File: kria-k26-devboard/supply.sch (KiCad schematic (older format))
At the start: 0 parts

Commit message: Progress on Debug sheet
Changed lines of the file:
@@
 F1 "usbc-socket.sch" 50
 F2 "PD_CC[1..2]" I L 3600 2800 50
-F3 "DBG_USB[0..1]" I L 3600 2900 50
-F4 "VBUS" I R 4700 2800 50
+F3 "VBUS" I R 4700 2800 50
+F4 "DBG_USB_P" I L 3600 3000 50
+F5 "DBG_USB_N" I L 3600 3100 50
 $EndSheet
 $Sheet
@@
 Text HLabel 3450 2800 0    50   Input ~ 0
 PD_CC[1..2]
-Text HLabel 3450 2900 0    50   Input ~ 0
-DBG_USB[0..1]
 Wire Wire Line
 	3450 2800 3600 2800
-Wire Wire Line
-	3600 2900 3450 2900
 Text HLabel 7550 3550 0    50   Input ~ 0
 VCCOEN_PS_M2C
@@
 Wire Bus Line
 	3400 4600 3600 4600
+Text HLabel 3450 3000 0    50   Input ~ 0
+DBG_USB_P
+Wire Wire Line
+	3450 3000 3600 3000
+Text HLabel 3450 3100 0    50   Input ~ 0
+DBG_USB_N
+Wire Wire Line
+	3450 3100 3600 3100
 $EndSCHEMATC

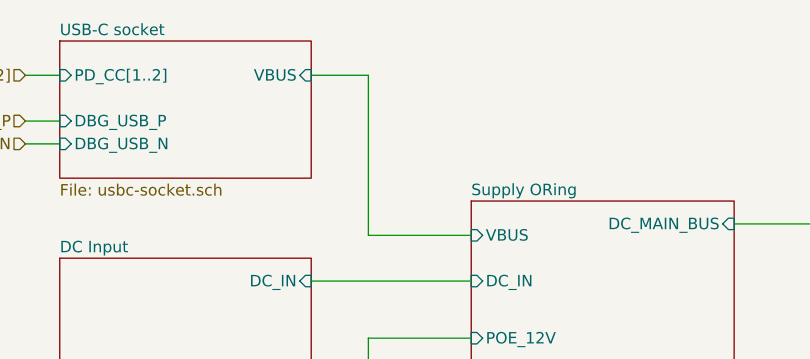
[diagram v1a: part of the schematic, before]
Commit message: Finished Debug and JTAG schematic
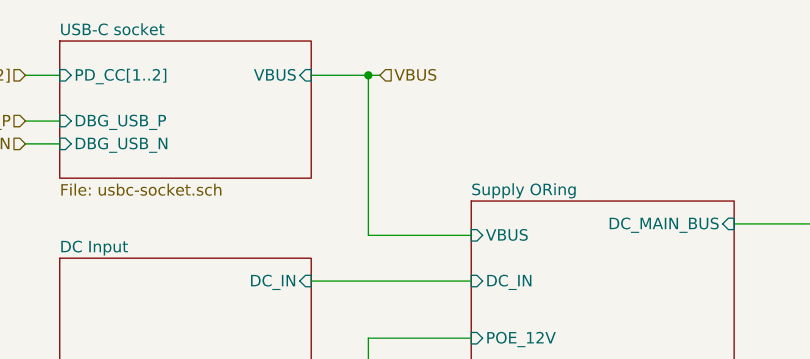
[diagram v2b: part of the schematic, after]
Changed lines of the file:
@@
 Wire Wire Line
 	3450 3100 3600 3100
+Text HLabel 5000 2800 2    50   Input ~ 0
+VBUS
+Wire Wire Line
+	4950 2800 5000 2800
+Connection ~ 4950 2800
 $EndSCHEMATC

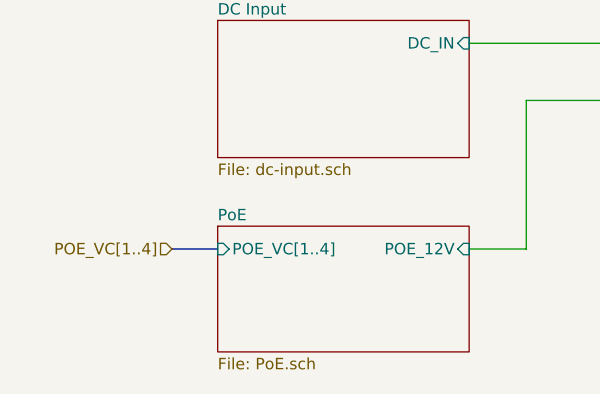
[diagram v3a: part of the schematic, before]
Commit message: Added second ETH interface, connect POE PSE
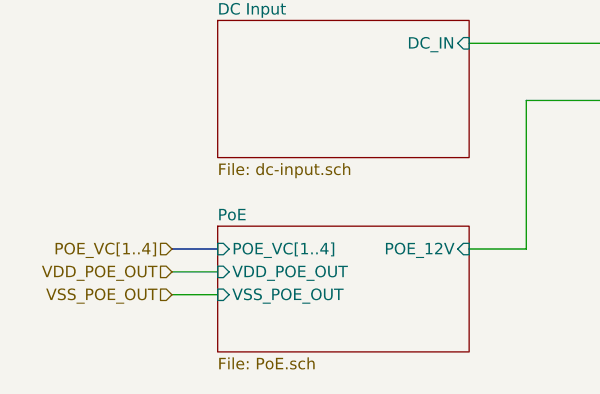
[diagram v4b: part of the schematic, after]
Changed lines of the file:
@@
 F2 "POE_12V" I R 4700 4600 50
 F3 "POE_VC[1..4]" I L 3600 4600 50
+F4 "VDD_POE_OUT" I L 3600 4700 50
+F5 "VSS_POE_OUT" I L 3600 4800 50
 $EndSheet
 $Sheet
@@
 	4950 2800 5000 2800
 Connection ~ 4950 2800
+Wire Wire Line
+	3600 4700 3400 4700
+Wire Wire Line
+	3600 4800 3400 4800
+Text HLabel 3400 4700 0    50   Input ~ 0
+VDD_POE_OUT
+Text HLabel 3400 4800 0    50   Input ~ 0
+VSS_POE_OUT
 $EndSCHEMATC

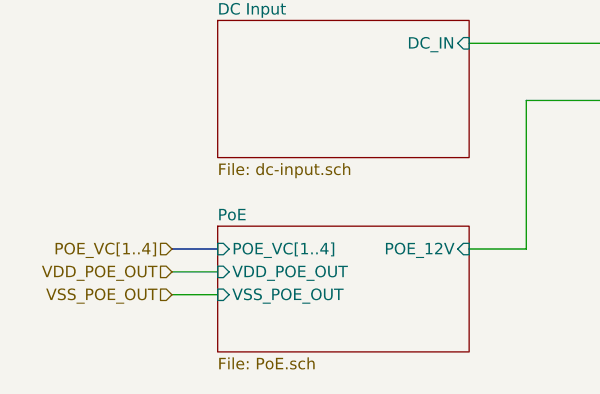
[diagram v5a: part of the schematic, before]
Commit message: Removed PoE PSE and second ETH interface
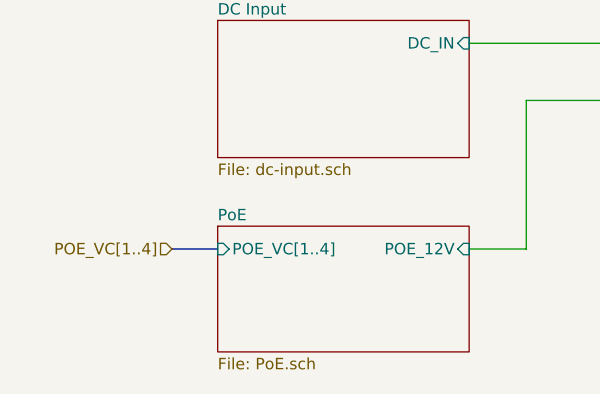
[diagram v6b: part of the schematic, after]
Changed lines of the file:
@@
 F2 "POE_12V" I R 4700 4600 50
 F3 "POE_VC[1..4]" I L 3600 4600 50
-F4 "VDD_POE_OUT" I L 3600 4700 50
-F5 "VSS_POE_OUT" I L 3600 4800 50
 $EndSheet
 $Sheet
@@
 	4950 2800 5000 2800
 Connection ~ 4950 2800
-Wire Wire Line
-	3600 4700 3400 4700
-Wire Wire Line
-	3600 4800 3400 4800
-Text HLabel 3400 4700 0    50   Input ~ 0
-VDD_POE_OUT
-Text HLabel 3400 4800 0    50   Input ~ 0
-VSS_POE_OUT
 $EndSCHEMATC

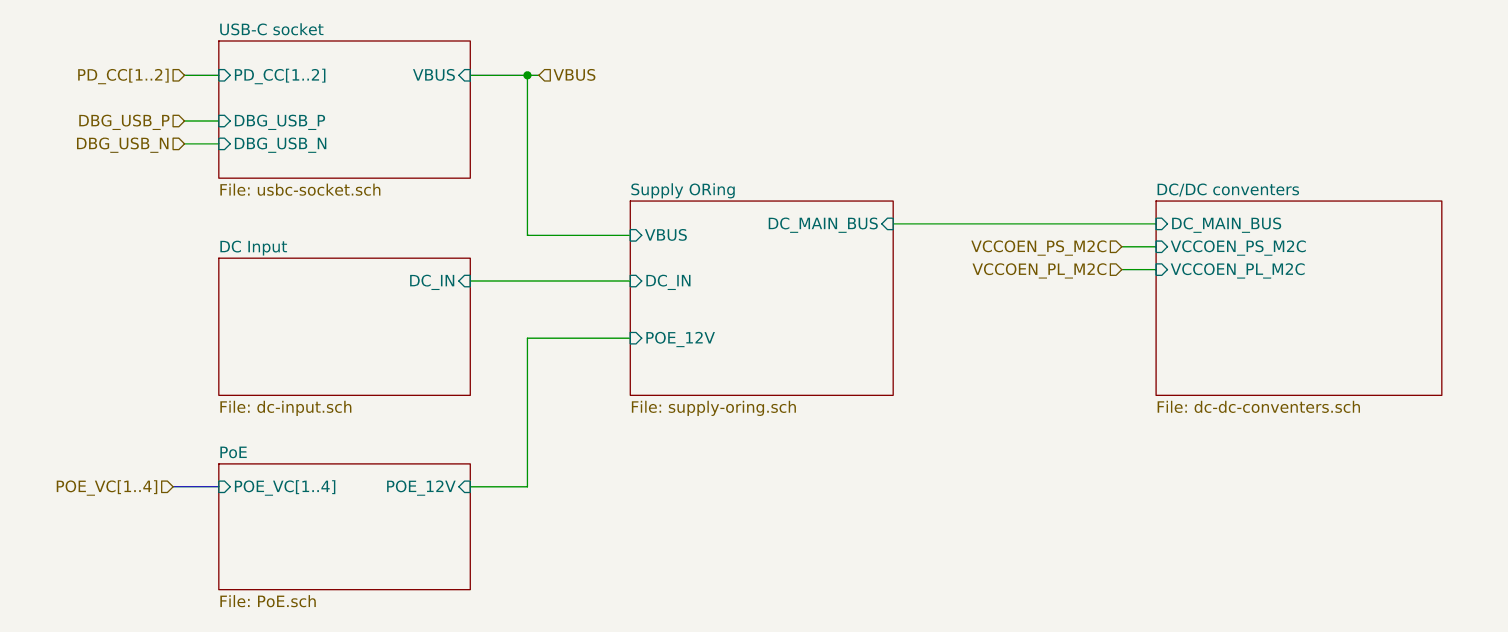
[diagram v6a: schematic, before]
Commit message: Added Led voltage indicator, fan circuit. Tidied up supply and SOM sheet
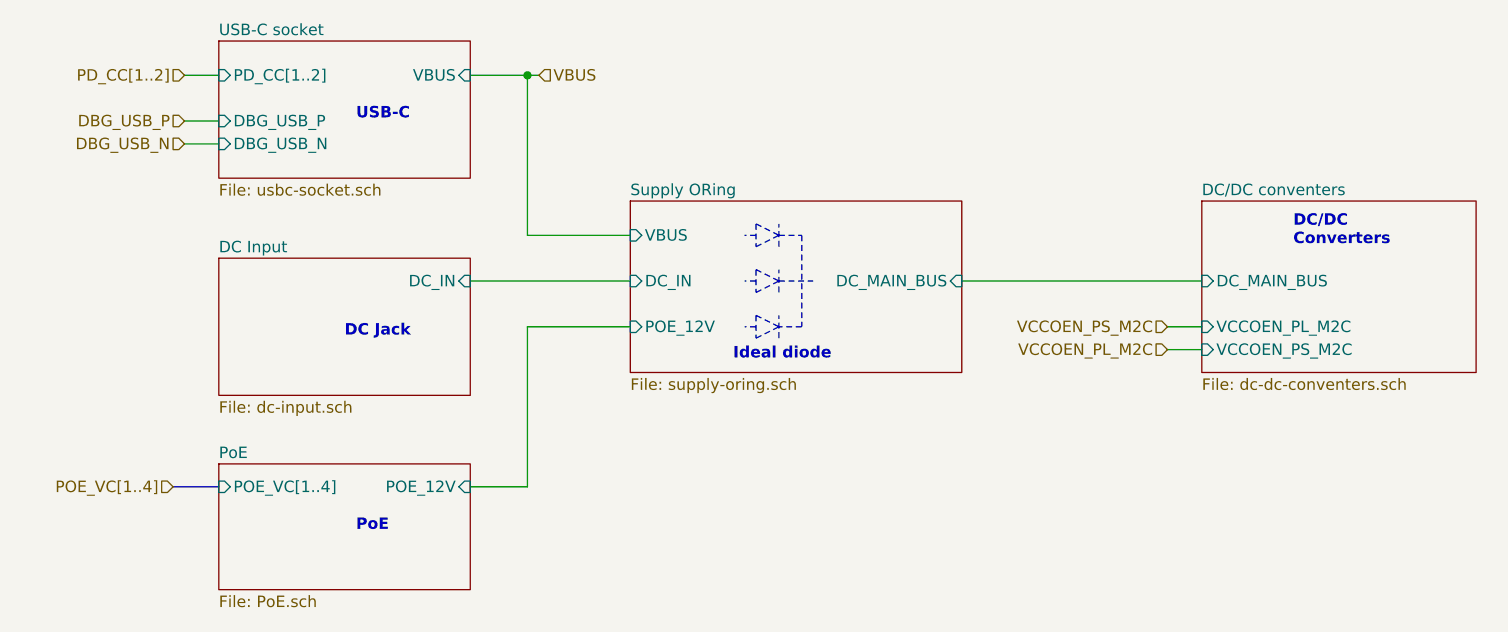
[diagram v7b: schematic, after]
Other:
- note added: "DC Jack"
- note added: "DC/DC\nConverters"
- note added: "Ideal diode"
- note added: "PoE"
- note added: "USB-C"
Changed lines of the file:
@@
 $EndSheet
 $Sheet
-S 7700 3350 1250 850
+S 7900 3350 1200 750
 U 6244F9D5
 F0 "DC/DC conventers" 50
 F1 "dc-dc-conventers.sch" 50
-F2 "DC_MAIN_BUS" I L 7700 3450 50
-F3 "VCCOEN_PS_M2C" I L 7700 3550 50
-F4 "VCCOEN_PL_M2C" I L 7700 3650 50
+F2 "DC_MAIN_BUS" I L 7900 3700 50
+F3 "VCCOEN_PS_M2C" I L 7900 4000 50
+F4 "VCCOEN_PL_M2C" I L 7900 3900 50
 $EndSheet
 $Sheet
-S 5400 3350 1150 850
+S 5400 3350 1450 750
 U 629B9728
 F0 "Supply ORing" 50
@@
 F2 "VBUS" I L 5400 3500 50
 F3 "DC_IN" I L 5400 3700 50
-F4 "POE_12V" I L 5400 3950 50
-F5 "DC_MAIN_BUS" I R 6550 3450 50
+F4 "POE_12V" I L 5400 3900 50
+F5 "DC_MAIN_BUS" I R 6850 3700 50
 $EndSheet
-Wire Wire Line
-	6550 3450 7700 3450
 $Sheet
 S 3600 2650 1100 600
@@
 	4700 3700 5400 3700
 Wire Wire Line
-	5400 3950 4950 3950
+	5400 3900 4950 3900
 Wire Wire Line
-	4950 3950 4950 4600
+	4950 3900 4950 4600
 Wire Wire Line
 	4950 4600 4700 4600
@@
 Wire Wire Line
 	3450 2800 3600 2800
-Text HLabel 7550 3550 0    50   Input ~ 0
+Text HLabel 7750 3900 0    50   Input ~ 0
 VCCOEN_PS_M2C
-Text HLabel 7550 3650 0    50   Input ~ 0
+Text HLabel 7750 4000 0    50   Input ~ 0
 VCCOEN_PL_M2C
 Wire Wire Line
-	7550 3550 7700 3550
+	7750 3900 7900 3900
 Wire Wire Line
-	7550 3650 7700 3650
+	7750 4000 7900 4000
 Text HLabel 3400 4600 0    50   Input ~ 0
 POE_VC[1..4]
@@
 	4950 2800 5000 2800
 Connection ~ 4950 2800
+Wire Notes Line style solid rgb(132, 132, 132)
+	5950 3850 5950 3950
+Wire Notes Line style solid rgb(132, 132, 132)
+	5950 3950 6050 3900
+Wire Notes Line style solid rgb(132, 132, 132)
+	5950 3850 6050 3900
+Wire Notes Line style solid rgb(132, 132, 132)
+	6050 3950 6050 3850
+Wire Notes Line style solid rgb(132, 132, 132)
+	5950 3650 5950 3750
+Wire Notes Line style solid rgb(132, 132, 132)
+	5950 3750 6050 3700
+Wire Notes Line style solid rgb(132, 132, 132)
+	5950 3650 6050 3700
+Wire Notes Line style solid rgb(132, 132, 132)
+	6050 3750 6050 3650
+Wire Notes Line style solid rgb(132, 132, 132)
+	5950 3450 5950 3550
+Wire Notes Line style solid rgb(132, 132, 132)
+	5950 3550 6050 3500
+Wire Notes Line style solid rgb(132, 132, 132)
+	5950 3450 6050 3500
+Wire Notes Line style solid rgb(132, 132, 132)
+	6050 3550 6050 3450
+Wire Notes Line style solid rgb(132, 132, 132)
+	6050 3500 6150 3500
+Wire Notes Line style solid rgb(132, 132, 132)
+	6150 3500 6150 3900
+Wire Notes Line style solid rgb(132, 132, 132)
+	6150 3900 6050 3900
+Wire Notes Line style solid rgb(132, 132, 132)
+	6050 3700 6200 3700
+Wire Notes Line style solid rgb(132, 132, 132)
+	5950 3700 5900 3700
+Wire Notes Line style solid rgb(132, 132, 132)
+	5950 3500 5900 3500
+Wire Notes Line style solid rgb(132, 132, 132)
+	5950 3900 5900 3900
+Text Notes 5850 4050 0    50   ~ 10
+Ideal diode
+Wire Wire Line
+	6850 3700 7900 3700
+Text Notes 4150 3950 0    50   ~ 10
+DC Jack
+Text Notes 4200 4800 0    50   ~ 10
+PoE
+Text Notes 4200 3000 0    50   ~ 10
+USB-C
+Text Notes 8300 3550 0    50   ~ 10
+DC/DC\nConverters
 $EndSCHEMATC

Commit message: Finished tidying up the schematic
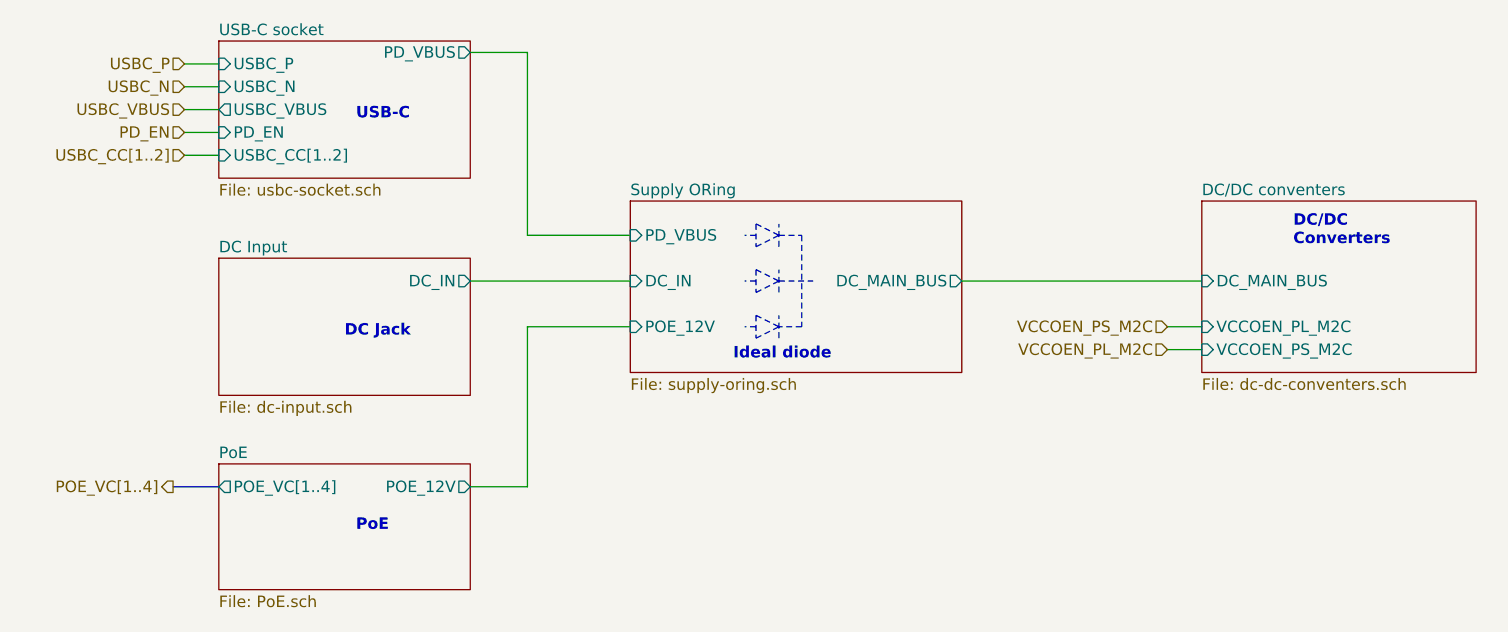
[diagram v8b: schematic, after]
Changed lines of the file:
@@
 $Descr A4 11693 8268
 encoding utf-8
-Sheet 2 19
+Sheet 14 19
 Title ""
 Date "2022-03-10"
@@
 F0 "PoE" 50
 F1 "PoE.sch" 50
-F2 "POE_12V" I R 4700 4600 50
-F3 "POE_VC[1..4]" I L 3600 4600 50
+F2 "POE_12V" O R 4700 4600 50
+F3 "POE_VC[1..4]" O L 3600 4600 50
 $EndSheet
 $Sheet
@@
 F0 "Supply ORing" 50
 F1 "supply-oring.sch" 50
-F2 "VBUS" I L 5400 3500 50
-F3 "DC_IN" I L 5400 3700 50
-F4 "POE_12V" I L 5400 3900 50
-F5 "DC_MAIN_BUS" I R 6850 3700 50
+F2 "DC_IN" I L 5400 3700 50
+F3 "POE_12V" I L 5400 3900 50
+F4 "DC_MAIN_BUS" O R 6850 3700 50
+F5 "PD_VBUS" I L 5400 3500 50
 $EndSheet
 $Sheet
@@
 F0 "USB-C socket" 50
 F1 "usbc-socket.sch" 50
-F2 "PD_CC[1..2]" I L 3600 2800 50
-F3 "VBUS" I R 4700 2800 50
-F4 "DBG_USB_P" I L 3600 3000 50
-F5 "DBG_USB_N" I L 3600 3100 50
+F2 "USBC_CC[1..2]" I L 3600 3150 50
+F3 "USBC_P" I L 3600 2750 50
+F4 "USBC_N" I L 3600 2850 50
+F5 "USBC_VBUS" O L 3600 2950 50
+F6 "PD_VBUS" O R 4700 2700 50
+F7 "PD_EN" I L 3600 3050 50
 $EndSheet
 $Sheet
@@
 F0 "DC Input" 50
 F1 "dc-input.sch" 50
-F2 "DC_IN" I R 4700 3700 50
+F2 "DC_IN" O R 4700 3700 50
 $EndSheet
 Wire Wire Line
-	4700 2800 4950 2800
-Wire Wire Line
-	4950 2800 4950 3500
+	4700 2700 4950 2700
 Wire Wire Line
 	4950 3500 5400 3500
@@
 Wire Wire Line
 	4950 4600 4700 4600
-Text HLabel 3450 2800 0    50   Input ~ 0
-PD_CC[1..2]
+Text HLabel 3450 3150 0    50   Input ~ 0
+USBC_CC[1..2]
 Wire Wire Line
-	3450 2800 3600 2800
+	3450 3150 3600 3150
 Text HLabel 7750 3900 0    50   Input ~ 0
 VCCOEN_PS_M2C
@@
 Wire Wire Line
 	7750 4000 7900 4000
-Text HLabel 3400 4600 0    50   Input ~ 0
+Text HLabel 3400 4600 0    50   Output ~ 0
 POE_VC[1..4]
 Wire Bus Line
 	3400 4600 3600 4600
-Text HLabel 3450 3000 0    50   Input ~ 0
-DBG_USB_P
+Text HLabel 3450 2750 0    50   Input ~ 0
+USBC_P
 Wire Wire Line
-	3450 3000 3600 3000
-Text HLabel 3450 3100 0    50   Input ~ 0
-DBG_USB_N
+	3450 2750 3600 2750
+Text HLabel 3450 2850 0    50   Input ~ 0
+USBC_N
 Wire Wire Line
-	3450 3100 3600 3100
-Text HLabel 5000 2800 2    50   Input ~ 0
-VBUS
-Wire Wire Line
-	4950 2800 5000 2800
-Connection ~ 4950 2800
+	3450 2850 3600 2850
+Text HLabel 3450 2950 0    50   Input ~ 0
+USBC_VBUS
 Wire Notes Line style solid rgb(132, 132, 132)
 	5950 3850 5950 3950
@@
 Text Notes 8300 3550 0    50   ~ 10
 DC/DC\nConverters
+Wire Wire Line
+	4950 2700 4950 3500
+Wire Wire Line
+	3450 2950 3600 2950
+Wire Wire Line
+	3600 3050 3450 3050
+Text HLabel 3450 3050 0    50   Input ~ 0
+PD_EN
 $EndSCHEMATC
